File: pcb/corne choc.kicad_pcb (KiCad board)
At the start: 2 copper layers, 265.7 x 87.7 mm, 167 parts, among them J1 MJ-4PP-9, J2 OLED, J3 MJ-4PP-9, J4 OLED, SW1 SW_PUSH, SW10 SW_PUSH, SW11 SW_PUSH, SW12 SW_PUSH, SW13 SW_PUSH, SW14 SW_PUSH, SW15 SW_PUSH, SW16 SW_PUSH, SW17 SW_PUSH, SW18 SW_PUSH, SW19 SW_PUSH, SW2 SW_PUSH, SW20 SW_PUSH, SW21 SW_PUSH, SW22 SW_PUSH, SW23 SW_PUSH, SW24 SW_PUSH, SW25 SW_PUSH, SW26 SW_PUSH, SW27 SW_PUSH, SW28 SW_PUSH, SW29 SW_PUSH, SW3 SW_PUSH, SW30 SW_PUSH, SW31 SW_PUSH, SW32 SW_PUSH, SW33 SW_PUSH, SW34 SW_PUSH, SW35 SW_PUSH, SW36 SW_PUSH, SW37 SW_PUSH, SW38 SW_PUSH, SW39 SW_PUSH, SW4 SW_PUSH, SW41 SW_PUSH, SW42 SW_PUSH, SW5 SW_PUSH, SW6 SW_PUSH, SW7 SW_PUSH, SW8 SW_PUSH, SW9 SW_PUSH, U1 ProMicro, U2 ProMicro

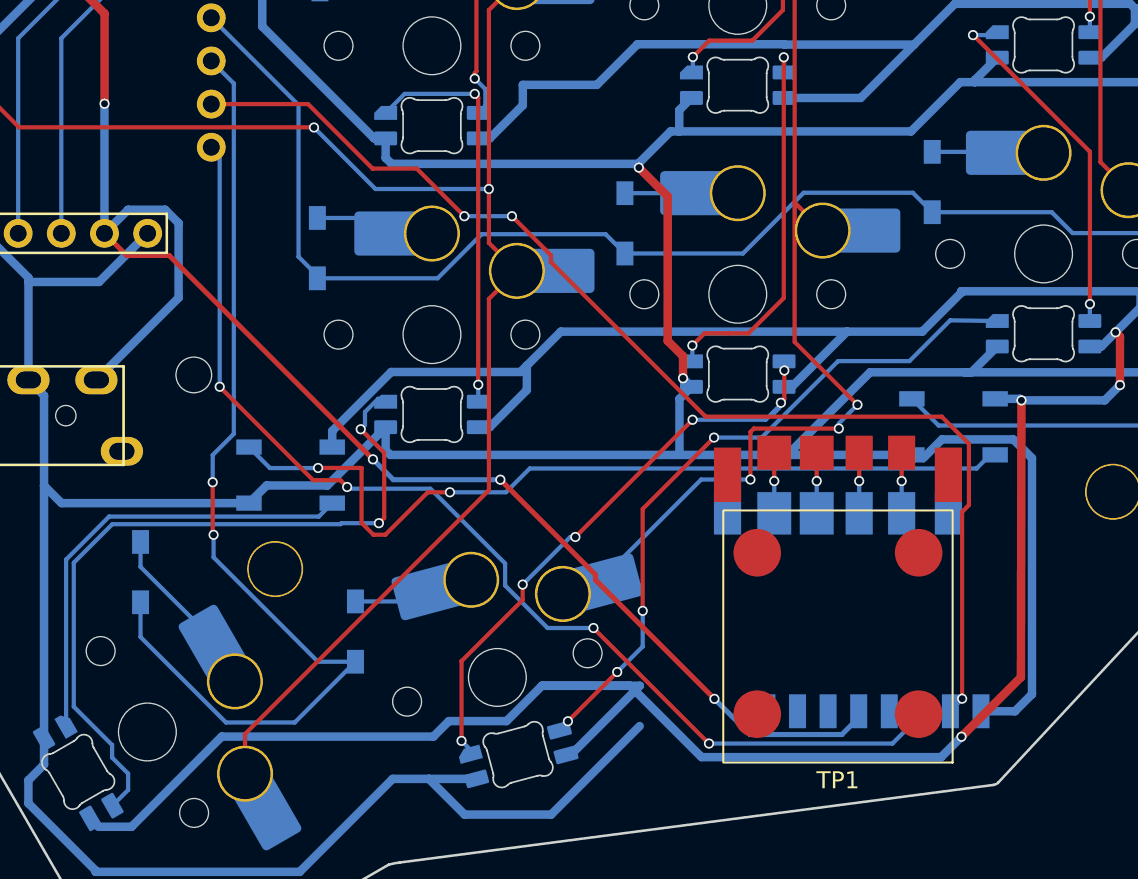
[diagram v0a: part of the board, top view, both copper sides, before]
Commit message: Driver footprint from holykeebs' top-view photo: 23 x 14.5 mm, wider host pads
The photo shows the detached driver is the full 14.5 mm control board and
confirms the sensor-link pad pitch and order. Driver moved to fit; routes now
name pads instead of coordinates; router keeps 0.3 mm from holes.
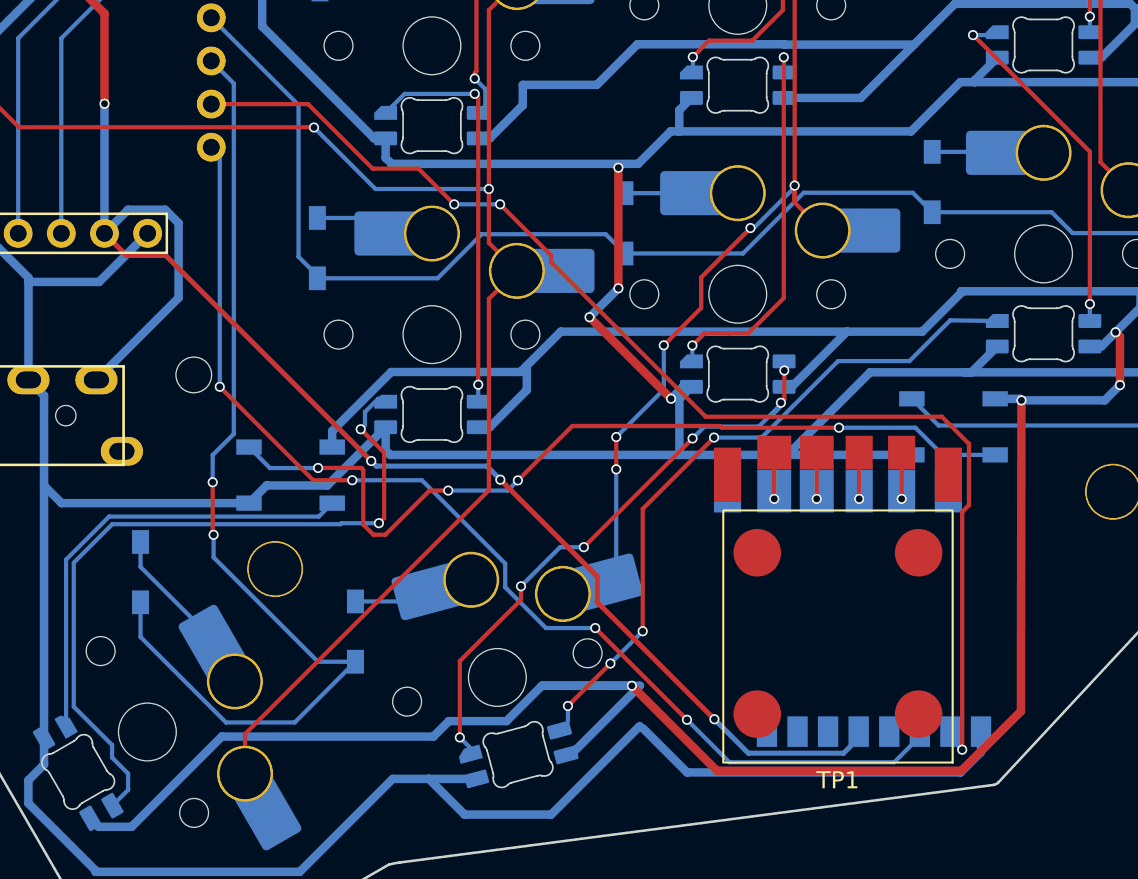
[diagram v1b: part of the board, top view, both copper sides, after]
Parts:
- moved TP2 0.15 mm to (206.7, 116.2)
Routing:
- net col4_r: track 143.0 -> 137.4 mm, vias 5 -> 7
- net TP_DATA: track 69.3 -> 72.6 mm
- net Net-(D44-K): track 555.7 -> 557.5 mm
- net GNDA: track 584.4 -> 586.1 mm, vias 4 -> 6
- net Net-(LED32-DOUT): track 49.9 -> 51.4 mm, vias 2 -> 4
- net VDD: track 145.4 -> 146.5 mm

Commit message: v2: wider inner edges, jacks at the top, split inner thumb keys, peaked top edges
Both halves widen 6.2 mm inward with the TRRS jacks facing the top edge; each
inner 1.5u thumb becomes two 1u keys at the same angle (new key on col2, with
diode and LED in the chain); edges sit 0.95 mm from the inner thumb keycaps;
top edges peak at the middle-finger column. New switch plate and FR4 bottom.
Routing is DRC-driven (autoconnect + maze); DRC matches upstream apart from
warnings.
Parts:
- added D45: D, kbd:D3_SMD_v2, B.Cu at (131.8, 115.8)
- added D46: D, kbd:D3_SMD_v2, B.Cu at (172.2, 102.9)
- added LED55: YS-SK6812MINI-E, PCM_marbastlib-various:LED_6028R, B.Cu at (144.1, 114.0)
- added LED56: YS-SK6812MINI-E, PCM_marbastlib-various:LED_6028R, B.Cu at (167.6, 114.0)
- added SW43: SW_PUSH, holykeebs:SW_choc_v1_HS_CPG135001S30_1u, B.Cu at (140.0, 111.6)
- added SW44: SW_PUSH, holykeebs:SW_choc_v1_HS_CPG135001S30_1u, B.Cu at (171.7, 111.6)
- SW21, SW42: footprint holykeebs:SW_choc_v1_HS_CPG135001S30_1.5u -> holykeebs:SW_choc_v1_HS_CPG135001S30_1u
- moved J3 48.4 mm to (162.3, 57.2), turned to 0 degrees
- moved J1 47.6 mm to (149.4, 57.2), turned to 0 degrees
- moved D42 26.5 mm to (180.3, 136.0), turned to -165 degrees
- moved LED54 22.8 mm to (184.8, 124.9), turned to 120 degrees
- moved SW42 15.2 mm to (180.7, 127.2), turned to 120 degrees
- moved TP2 12.4 mm to (219.1, 116.1)
- moved D22 12.4 mm to (278.7, 64.4)
- moved D29 12.4 mm to (260.7, 79.5)
- moved D35 12.4 mm to (260.0, 98.3)
- moved LED28 12.4 mm to (276.4, 73.8)
- moved LED31 12.4 mm to (276.2, 90.9)
- moved ? 12.4 mm to (204.5, 72.0)
- moved D25 12.4 mm to (224.5, 56.6)
- moved D26 12.4 mm to (206.9, 59.5)
- moved D27 12.4 mm to (188.2, 60.9)
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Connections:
- LED27 pad 2: Net-(LED24-DIN) -> Net-(LED27-DOUT)
- LED54 pad 2: Net-(LED51-DIN) -> Net-(LED54-DOUT)
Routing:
- net GNDA: track 586.1 -> 527.3 mm
- net col2_r: track 142.2 -> 185.5 mm
- net data: track 45.0 -> 8.02 mm
- net col2: track 122.0 -> 154.2 mm, vias 2 -> 3
- net data_r: track 62.1 -> 38.7 mm
- net Net-(LED54-DOUT): track 0.00 -> 21.9 mm, vias 0 -> 2
- net row3_r: track 59.5 -> 78.9 mm, vias 2 -> 6
- net VCC: track 65.9 -> 84.8 mm, vias 0 -> 2
- net Net-(LED50-DOUT): track 33.8 -> 50.8 mm, vias 6 -> 8
- net Net-(LED27-DOUT): track 0.00 -> 13.5 mm
- net VDD: track 146.5 -> 133.8 mm, vias 5 -> 3
- net Net-(D44-K): track 557.5 -> 545.6 mm, vias 6 -> 11
- net col0: track 156.1 -> 167.6 mm, vias 1 -> 7
- net Net-(D43-K): track 582.7 -> 593.7 mm, vias 2 -> 5
- net Net-(LED51-DIN): track 43.9 -> 33.4 mm, vias 2 -> 4
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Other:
- board size 265.7 x 87.7 mm -> 278.1 x 88.2 mm

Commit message: v2.1: thumb arc, key-following edges, roomier trackpoint
- Thumb keys on one arc on both halves (0/15/30 degrees); the split inner
  keys turn like the others and stack one row apart (tools/thumbs.py).
- Edge round the thumbs redrawn from the keys: 0.95 mm from the inner
  keycaps, one level line under the middle and outer keys, and a 60-degree
  outer slant cornered off the trackpoint sensor. Halves identical.
- Trackpoint stem 3.4 mm lower in the same board footprint.
- Holykeebs and Corne logos removed.
- Separate right switch plate with an opening for the sensor.
- Router stops on the copper it is joining; ground islands are joined to
  the main ground; sensor links routed like other nets.
- Renders use KLP Lame keycaps; tools/demo.sh rebuilds them.
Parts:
- removed G*** (x4): LOGO, kbd:corne-logo-horizontal-mask
- removed REF** (x2): logo big, holykeebs:logo .5x
- moved D21 13.4 mm to (135.5, 136.0), turned to -105 degrees
- moved D46 13.3 mm to (163.1, 112.6), turned to 105 degrees
- moved D45 13.3 mm to (144.0, 121.2), turned to -105 degrees
- moved LED54 7.30 mm to (182.7, 131.9), turned to 30 degrees
- moved LED56 7.30 mm to (174.2, 117.1), turned to 30 degrees
- moved LED27 6.00 mm to (133.7, 123.7), turned to 150 degrees
- moved LED55 5.31 mm to (142.2, 109.0), turned to 150 degrees
- moved D42 3.92 mm to (176.4, 135.6), turned to 105 degrees
- moved TP1 3.39 mm to (219.1, 120.9)
- moved SW43 1.46 mm to (139.8, 113.1), turned to 150 degrees
- moved SW44 1.46 mm to (171.9, 113.1), turned to 30 degrees
- moved SW42 0.68 mm to (180.4, 127.8), turned to 30 degrees
- moved SW21 0.68 mm to (131.3, 127.8), turned to 150 degrees
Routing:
- net Net-(D43-K): track 593.7 -> 520.6 mm, vias 5 -> 3
- net GND: track 594.4 -> 574.6 mm, vias 12 -> 14
- net Net-(LED50-DOUT): track 50.8 -> 36.0 mm, vias 8 -> 2
- net Net-(LED52-DIN): track 44.2 -> 56.2 mm
- net GNDA: track 527.3 -> 515.4 mm, vias 6 -> 4
- net col0_r: track 185.1 -> 175.0 mm
- net Net-(LED32-DOUT): track 55.8 -> 45.6 mm
- net col5: track 72.6 -> 82.0 mm
- net col2_r: track 185.5 -> 176.2 mm, vias 2 -> 3
- net row3_r: track 78.9 -> 87.5 mm, vias 6 -> 2
- net col5_r: track 113.3 -> 105.8 mm
- net Net-(LED24-DIN): track 28.0 -> 20.7 mm
- net TP_DATA: track 70.2 -> 77.4 mm, vias 3 -> 2
- net row3: track 108.6 -> 115.1 mm, vias 4 -> 3
- net data_r: track 38.7 -> 32.7 mm
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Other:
- board size 278.1 x 88.2 mm -> 278.1 x 88.4 mm
